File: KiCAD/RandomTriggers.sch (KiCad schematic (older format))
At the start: 37 parts, among them Q1 2N3904, Q2 2N3904, U1 TL072, U2 TL072

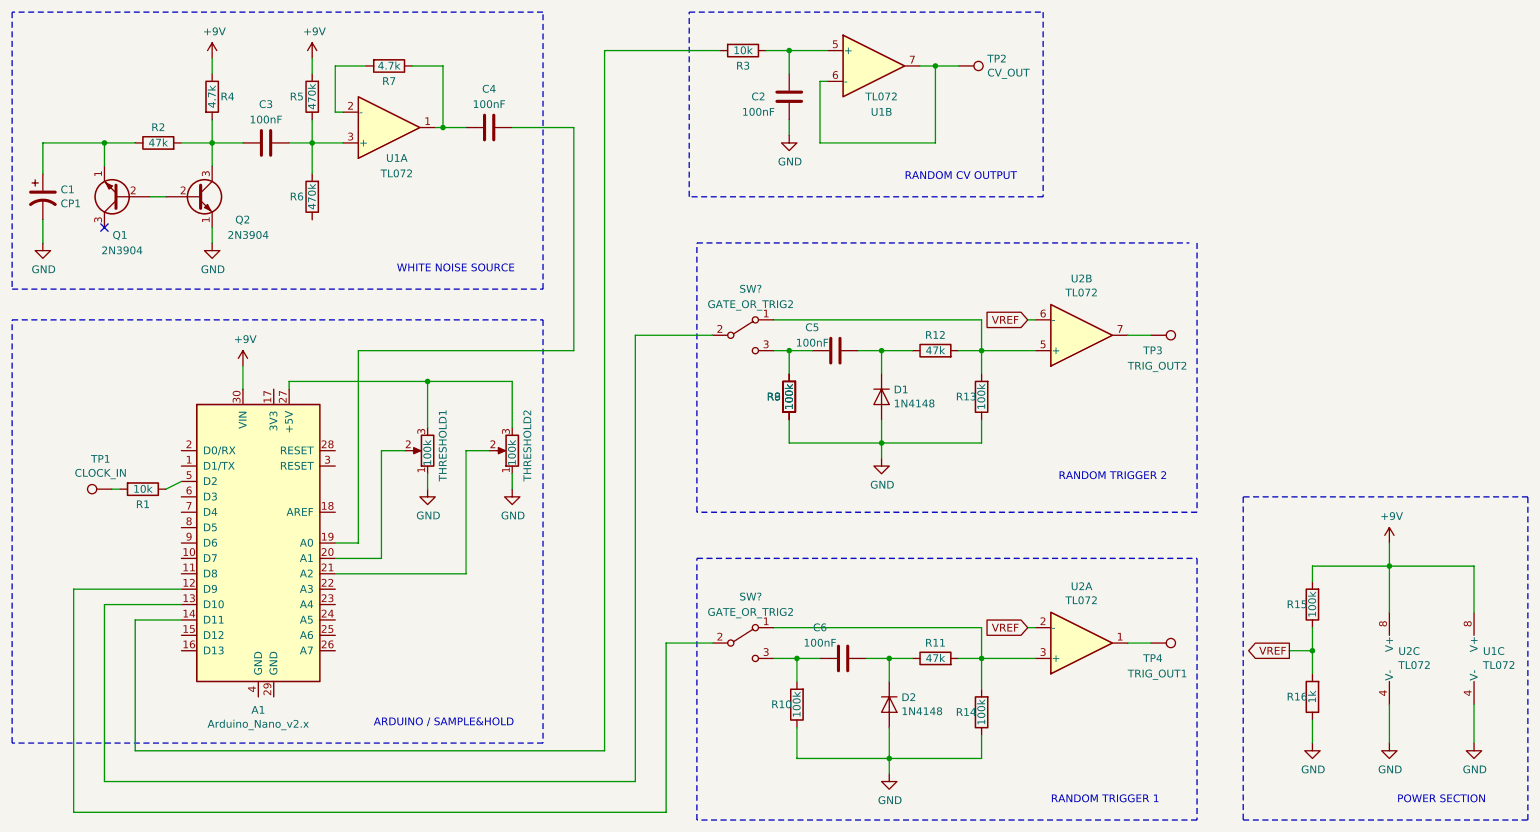
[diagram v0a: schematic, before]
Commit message: Removed white noise section
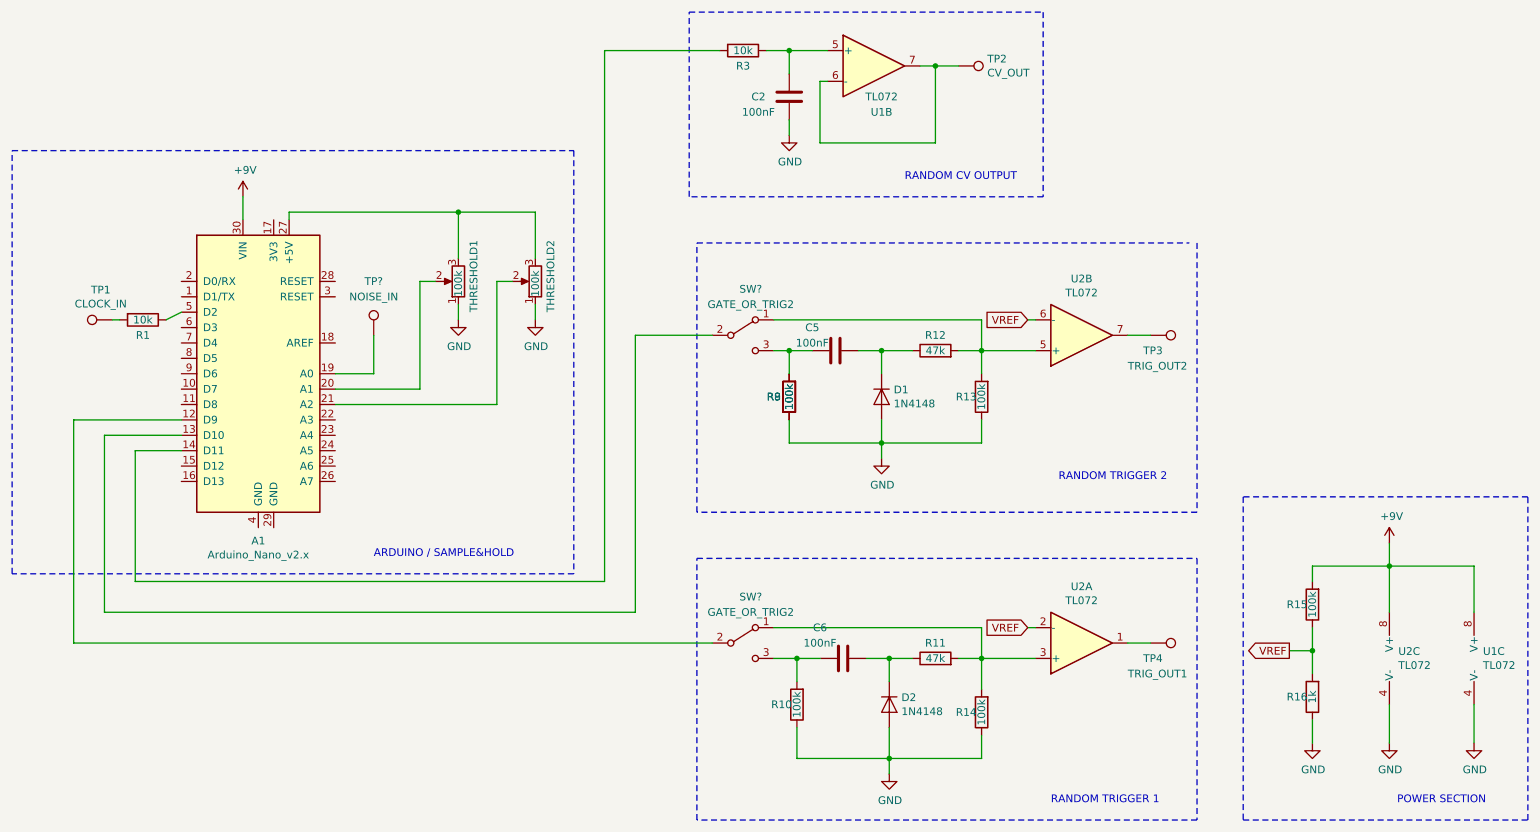
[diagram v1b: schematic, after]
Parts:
- removed C1: CP1, symbol Device:CP1
- removed C3, C4: 100nF, symbol Device:C
- removed Q1, Q2: 2N3904, Package_TO_SOT_THT:TO-92_Inline, symbol Transistor_BJT:2N3904
- removed R2: 47k, symbol Device:R
- removed R4, R7: 4.7k, symbol Device:R
- removed R5, R6: 470k, symbol Device:R
- removed unit 1 of U1
- added TP?: NOISE_IN, symbol Connector:TestPoint
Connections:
- net at A1.19 (A0): now also TP?.1
- no-connect marks 1 -> 0
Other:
- note removed: "WHITE NOISE SOURCE"
- moved on the sheet: A1, R1, THRESHOLD1, THRESHOLD2, TP1

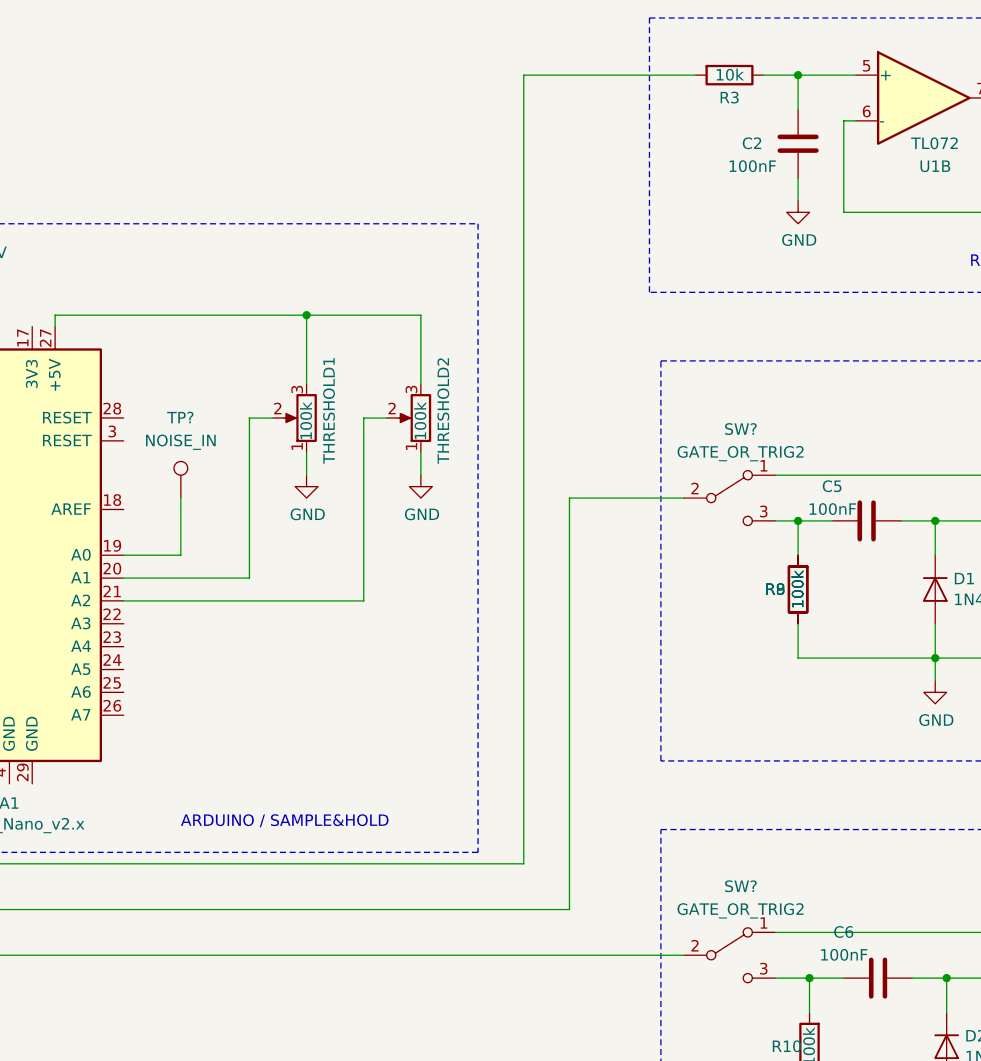
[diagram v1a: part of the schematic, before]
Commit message: Added picture of panel
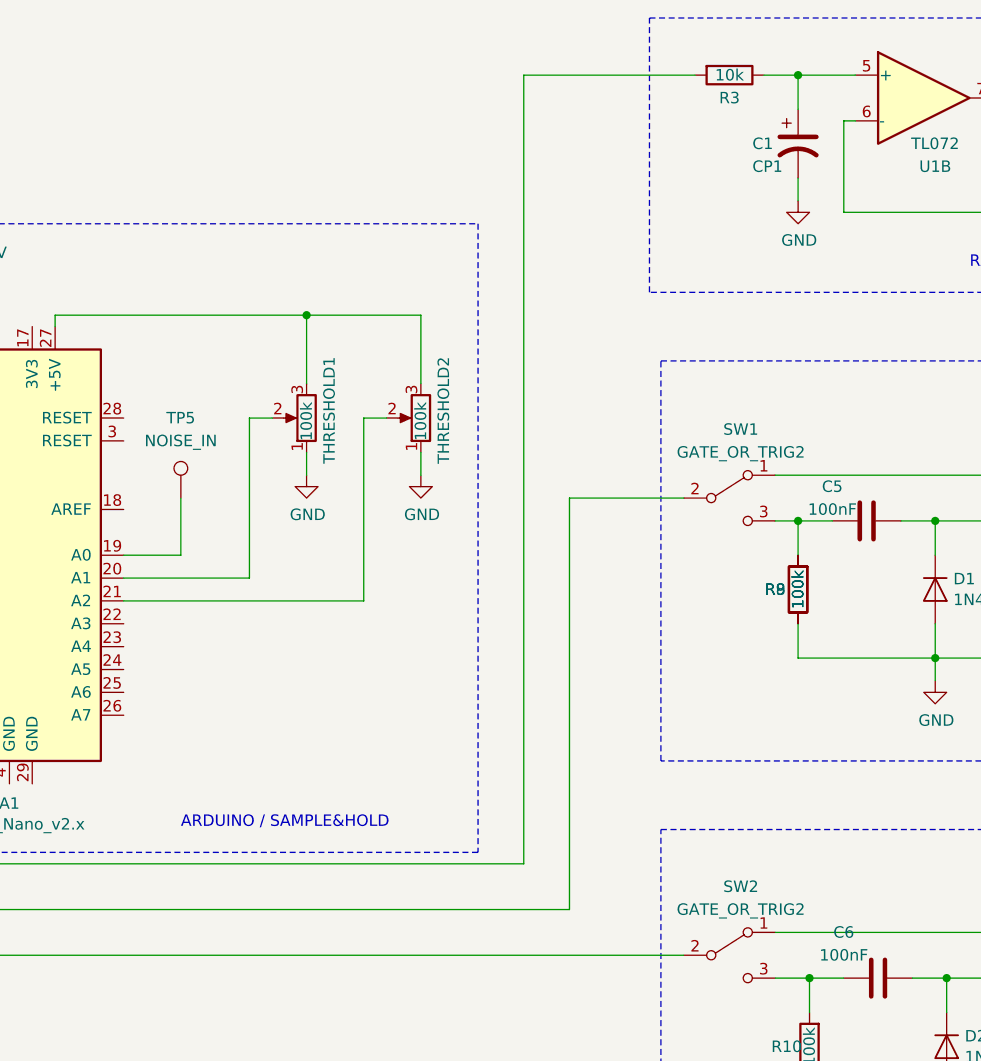
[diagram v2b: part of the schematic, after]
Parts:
- removed C2: 100nF, symbol Device:C
- added C1: CP1, symbol Device:CP1
- gave numbers to parts that had none: 3
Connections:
- net GND: now also C1.2
- net at R3.1, U1.5 (+): now also C1.1
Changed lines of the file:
@@
-$EndComp
-$Comp
-L Device:C C2
-U 1 1 60A1B015
-P 6200 1550
-F 0 "C2" H 6400 1550 50  0000 C CNN
-F 1 "100nF" H 6400 1650 50  0000 C CNN
-F 2 "" H 6238 1400 50  0001 C CNN
-F 3 "~" H 6200 1550 50  0001 C CNN
-	1    6200 1550
-	-1   0    0    1
 $EndComp
 $Comp
@@
 ARDUINO / SAMPLE&HOLD
 $Comp
-L Switch:SW_SPDT SW?
+L Switch:SW_SPDT SW1
 U 1 1 60BE52CD
 P 5900 3100
-F 0 "SW?" H 5950 3400 50  0000 C CNN
+F 0 "SW1" H 5950 3400 50  0000 C CNN
 F 1 "GATE_OR_TRIG2" H 5950 3300 50  0000 C CNN
 F 2 "" H 5900 3100 50  0001 C CNN
@@
 	5200 3100 5200 4900
 $Comp
-L Switch:SW_SPDT SW?
+L Switch:SW_SPDT SW2
 U 1 1 60C16A15
 P 5900 5100
-F 0 "SW?" H 5950 5400 50  0000 C CNN
+F 0 "SW2" H 5950 5400 50  0000 C CNN
 F 1 "GATE_OR_TRIG2" H 5950 5300 50  0000 C CNN
 F 2 "" H 5900 5100 50  0001 C CNN
@@
 	1550 5100 5700 5100
 $Comp
-L Connector:TestPoint TP?
+L Connector:TestPoint TP5
 U 1 1 60A82053
 P 3500 3100
-F 0 "TP?" H 3500 3450 50  0000 C CNN
+F 0 "TP5" H 3500 3450 50  0000 C CNN
 F 1 "NOISE_IN" H 3500 3350 50  0000 C CNN
 F 2 "" H 3700 3100 50  0001 C CNN
@@
 Wire Wire Line
 	3500 3100 3500 3350
+$Comp
+L Device:CP1 C1
+U 1 1 609FBE08
+P 6200 1550
+F 0 "C1" H 6000 1550 50  0000 L CNN
+F 1 "CP1" H 6000 1450 50  0000 L CNN
+F 2 "" H 6200 1550 50  0001 C CNN
+F 3 "~" H 6200 1550 50  0001 C CNN
+	1    6200 1550
+	1    0    0    -1
+$EndComp
 $EndSCHEMATC
